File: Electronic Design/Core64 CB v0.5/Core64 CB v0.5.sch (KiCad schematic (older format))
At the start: 36 parts, among them J1 TSM-116-03-T-SV‎, J2 TSM-116-03-T-SV‎, U1 SI7210-B-01, U2 SI7210-B-02, U3 SI7210-B-03, U4 SI7210-B-04, U5 LTR-329ALS-01, U6 TS3A4751PWR, U7 TS3A4751PWR, X1 SFH11-NBPC-D03-ST-BK

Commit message: Core board redline refinement
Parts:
- added R1, R2, R3, R4: 10K, Resistor_SMD:R_0805_2012Metric, symbol Device:R_Small
- C5: value 1uF -> 0.1uF
- J1, J2: value TSM-116-03-T-SV‎ -> Digi-Key 77311-420-36LF-ND; footprint Connector_PinHeader_2.54mm:PinHeader_1x16_P2.54mm_Vertical_SMD_and_TH_Pin1Right -> Connector_PinHeader_2.54mm:PinHeader_1x18_P2.54mm_Vertical_SMD_and_TH_Pin1Right; symbol Connector:Conn_01x16_Male -> Connector:Conn_01x18_Male
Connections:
- wire segments 183 -> 201
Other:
- note added: "AMBIENT LIGHT SENSOR I2C 0x29"
- note added: "NOTE: These GPIO will be\nused by Core Plane Select\nif that option is enabled."
- note added: "REQUIRED: CONFIGURE FOR ONE CORE PLANE"
- note added: "SILKSCREEN:\n5V0\nGND\nXT3,7\nXT2,6\nXT1,5\nXT0,4\nXB0\nXB1\nXB2\nXB3\nXB4\nXB5\nXB6\nXB7\nP1/IO1\nP2/IO2\nP3\nP4"
- note added: "SILKSCREEN:\nLSIG\nUSER\nYL0\nYL1\nYL2\nYL3\nYL4,6\nYL5,7\nSEN1\nSEN2\nSCL\nSDA\n3V3\nGNDD\nP8\nP7\nP6\nP5"
- note added: "STEP 3: Install two quad switches\nand two decoupling caps."
- note added: "STEP 4: Modify sense wire\nrouting through connectors."
- note added: "STEP 5 (LOGIC BOARD):\nSee instructions on Logic Board."
- note removed: "AUTOMATIC LIGHT SENSOR I2C 0x29"
- note removed: "Ceramic"
- note removed: "DEFAULT FOR ONE CORE PLANE ONLY"
- note removed: "SILKSCREEN:\nXT3,7\nXT2,6\nXT1,5\nXT0,4\nXB0\nXB1\nXB2\nXB3\nXB4\nXB5\nXB6\nXB7\nP1/IO1\nP2/IO2\nP3\nP4"
- note removed: "SILKSCREEN:\nYL0\nYL1\nYL2\nYL3\nYL4,6\nYL5,7\nSEN1\nSEN2\nSCL\nSDA\n3V3\nGNDD\nP8\nP7\nP6\nP5"
- note removed: "STEP 3:\nInstall two quad switches and two decoupling caps."
- moved on the sheet: C1, C5, X1

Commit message: Update core grid to 6.75mm square
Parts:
- CM1: footprint Core_Memory_8x8_Array:core_64_x6.7_y6.5mm_v0.3_front_facing -> Core_Memory_8x8_Array:core_64_6.75mm_square_v0.5_front_facing
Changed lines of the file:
@@
 F 0 "CM1" H 3650 2500 50  0000 C CNN
 F 1 "Core_Memory_8x8_Array_Front_Facing" H 4300 900 50  0000 C CNN
-F 2 "Core_Memory_8x8_Array:core_64_x6.7_y6.5mm_v0.3_front_facing" H 4350 1900 50  0001 C CNN
+F 2 "Core_Memory_8x8_Array:core_64_6.75mm_square_v0.5_front_facing" H 4350 1900 50  0001 C CNN
 F 3 "" H 4350 1900 50  0001 C CNN
 	1    4300 1850

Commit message: Update CB to be compatible with LM V0.1
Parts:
- J1, J2: footprint Connector_PinHeader_2.54mm:PinHeader_1x18_P2.54mm_Vertical_SMD_and_TH_Pin1Right -> Connector_PinHeader_2.54mm:PinHeader_1x20_P2.54mm_Vertical_SMD_and_TH_Pin1Right; symbol Connector:Conn_01x18_Male -> Connector:Conn_01x20_Male
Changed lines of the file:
@@
 Text GLabel 3950 900  1    50   Input ~ 0
 XT0-4
+Text GLabel 6700 1750 0    50   Output ~ 0
+XB3
+Text GLabel 6700 1650 0    50   Output ~ 0
+XB2
+Text GLabel 6700 1550 0    50   Output ~ 0
+XB1
+Text GLabel 6700 1450 0    50   Output ~ 0
+XB0
 Text GLabel 6700 1850 0    50   Output ~ 0
-XB3
-Text GLabel 6700 1750 0    50   Output ~ 0
-XB2
-Text GLabel 6700 1650 0    50   Output ~ 0
-XB1
-Text GLabel 6700 1550 0    50   Output ~ 0
-XB0
+XB4
 Text GLabel 6700 1950 0    50   Output ~ 0
-XB4
+XB5
 Text GLabel 6700 2050 0    50   Output ~ 0
-XB5
+XB6
 Text GLabel 6700 2150 0    50   Output ~ 0
-XB6
-Text GLabel 6700 2250 0    50   Output ~ 0
 XB7
-Text GLabel 6700 1450 0    50   Output ~ 0
+Text GLabel 6700 1350 0    50   Output ~ 0
 H_XT0-4
-Text GLabel 6700 1350 0    50   Output ~ 0
+Text GLabel 6700 1250 0    50   Output ~ 0
 H_XT1-5
-Text GLabel 6700 1250 0    50   Output ~ 0
+Text GLabel 6700 1150 0    50   Output ~ 0
 H_XT2-6
-Text GLabel 6700 1150 0    50   Output ~ 0
+Text GLabel 6700 1050 0    50   Output ~ 0
 H_XT3-7
 Wire Wire Line
@@
 Connection ~ 4250 1000
 Wire Wire Line
+	6700 1050 6950 1050
+Wire Wire Line
 	6700 1150 6950 1150
 Wire Wire Line
@@
 Wire Wire Line
 	6700 1350 6950 1350
-Wire Wire Line
-	6700 1450 6950 1450
 Text GLabel 3600 2200 0    50   Input ~ 0
 YL7
@@
 Text GLabel 3600 1500 0    50   Input ~ 0
 YL0
+Text GLabel 2150 1200 2    50   Output ~ 0
+H_YL1
+Text GLabel 2150 1100 2    50   Output ~ 0
+H_YL0
 Text GLabel 2150 1300 2    50   Output ~ 0
-H_YL1
-Text GLabel 2150 1200 2    50   Output ~ 0
-H_YL0
+H_YL2
 Text GLabel 2150 1400 2    50   Output ~ 0
-H_YL2
+H_YL3
 Text GLabel 2150 1500 2    50   Output ~ 0
-H_YL3
+YL4
 Text GLabel 2150 1600 2    50   Output ~ 0
-YL4
+YL5
 Text GLabel 2150 1700 2    50   Output ~ 0
-YL5
+YL6
 Text GLabel 2150 1800 2    50   Output ~ 0
-YL6
-Text GLabel 2150 1900 2    50   Output ~ 0
 YL7
 Wire Wire Line
-	2100 1600 2100 1800
-Wire Wire Line
-	2100 1800 2150 1800
-Wire Wire Line
-	2150 1200 1500 1200
+	2100 1500 2100 1700
+Wire Wire Line
+	2100 1700 2150 1700
+Wire Wire Line
+	2150 1100 1500 1100
+Wire Wire Line
+	1500 1200 2150 1200
 Wire Wire Line
 	1500 1300 2150 1300
 Wire Wire Line
-	1500 1400 2150 1400
-Wire Wire Line
-	2150 1500 1500 1500
-Wire Wire Line
-	2150 1600 2100 1600
-Wire Wire Line
-	2100 1600 1500 1600
-Connection ~ 2100 1600
+	2150 1400 1500 1400
+Wire Wire Line
+	2150 1500 2100 1500
+Wire Wire Line
+	2100 1500 1500 1500
+Connection ~ 2100 1500
 Wire Wire Line
 	5350 1900 5000 1900
@@
 	5000 2200 5050 2200
 Wire Wire Line
-	2050 1900 2150 1900
-Wire Wire Line
-	2050 1700 2050 1900
-Wire Wire Line
-	2150 1700 2050 1700
+	2050 1800 2150 1800
+Wire Wire Line
+	2050 1600 2050 1800
+Wire Wire Line
+	2150 1600 2050 1600
 Text Notes 1150 2550 2    50   ~ 0
 SILKSCREEN:\nLSIG\nUSER\nYL0\nYL1\nYL2\nYL3\nYL4,6\nYL5,7\nSEN1\nSEN2\nSCL\nSDA\n3V3\nGNDD\nP8\nP7\nP6\nP5
 Wire Wire Line
-	2050 1700 1500 1700
-Connection ~ 2050 1700
-Wire Wire Line
-	6700 2250 6950 2250
+	2050 1600 1500 1600
+Connection ~ 2050 1600
 Wire Wire Line
 	6700 2150 6950 2150
-$Comp
-L Connector:Conn_01x18_Male J2
+Wire Wire Line
+	6700 2050 6950 2050
+$Comp
+L Connector:Conn_01x20_Male J2
 U 1 1 5E723F12
 P 7150 1750
 F 0 "J2" H 7150 2700 50  0000 C CNN
 F 1 "Digi-Key 77311-420-36LF-ND" H 8000 2700 50  0000 C CNN
-F 2 "Connector_PinHeader_2.54mm:PinHeader_1x18_P2.54mm_Vertical_SMD_and_TH_Pin1Right" H 7150 1750 50  0001 C CNN
+F 2 "Connector_PinHeader_2.54mm:PinHeader_1x20_P2.54mm_Vertical_SMD_and_TH_Pin1Right" H 7150 1750 50  0001 C CNN
 F 3 "~" H 7150 1750 50  0001 C CNN
 	1    7150 1750
@@
 	3850 2550 3850 2500
 Wire Wire Line
+	6950 1450 6700 1450
+Wire Wire Line
 	6950 1550 6700 1550
 Wire Wire Line
 	6950 1650 6700 1650
 Wire Wire Line
-	6950 1750 6700 1750
-Wire Wire Line
-	6700 1850 6950 1850
-Wire Wire Line
-	6950 1950 6700 1950
-Wire Wire Line
-	6700 2050 6950 2050
-Text GLabel 1650 1900 2    50   Input ~ 0
+	6700 1750 6950 1750
+Wire Wire Line
+	6950 1850 6700 1850
+Wire Wire Line
+	6700 1950 6950 1950
+Text GLabel 1650 1800 2    50   Input ~ 0
 SENSE1
-Text GLabel 1650 1800 2    50   Input ~ 0
+Text GLabel 1650 1700 2    50   Input ~ 0
 SENSE2
 Wire Wire Line
@@
 	3550 2450 3500 2450
 Wire Wire Line
-	1650 1900 1500 1900
-Wire Wire Line
-	2450 2300 2450 2400
-Wire Wire Line
-	1500 2200 1650 2200
-Wire Wire Line
-	1500 2300 2450 2300
-Wire Wire Line
-	1500 2400 1900 2400
-Wire Wire Line
-	1900 2500 1500 2500
-Wire Wire Line
-	1500 2600 1900 2600
-Wire Wire Line
-	1900 2700 1500 2700
-Wire Wire Line
-	1500 1800 1650 1800
+	1650 1800 1500 1800
+Wire Wire Line
+	2450 2200 2450 2300
+Wire Wire Line
+	1500 2100 1650 2100
+Wire Wire Line
+	1500 2200 2450 2200
+Wire Wire Line
+	1500 2300 1900 2300
+Wire Wire Line
+	1900 2400 1500 2400
+Wire Wire Line
+	1500 2500 1900 2500
+Wire Wire Line
+	1900 2600 1500 2600
+Wire Wire Line
+	1500 1700 1650 1700
+Text GLabel 1650 1900 2    50   BiDi ~ 0
+I2C_CLOCK
 Text GLabel 1650 2000 2    50   BiDi ~ 0
-I2C_CLOCK
-Text GLabel 1650 2100 2    50   BiDi ~ 0
 I2C_DATA
 Wire Wire Line
+	1500 1900 1650 1900
+Wire Wire Line
 	1500 2000 1650 2000
-Wire Wire Line
-	1500 2100 1650 2100
-Text GLabel 1650 2200 2    50   Input ~ 0
+Text GLabel 1650 2100 2    50   Input ~ 0
 3V3_800mA
 Text Notes 1650 4500 0    50   ~ 0
@@
 Text Notes 3300 4700 0    50   ~ 0
 I2C configurable hall sensors, not just a switch.\nSilicon Labs SI7210-B-01-IVR through 04-IVR\nLow (push-pull) up to 20 mT, SOT23-5\nhttps://www.digikey.com/product-detail/en/silicon-labs/SI7210-B-04-IVR/336-4129-1-ND/7648844
-Text Notes 2350 2850 0    50   ~ 0
+Text Notes 2350 2750 0    50   ~ 0
 DIGITAL\nLOGIC\nGROUND
 $Comp
@@
 Wire Wire Line
 	9050 1400 9200 1400
-Text GLabel 6950 2800 2    50   Input ~ 0
+Text GLabel 6950 2850 2    50   Input ~ 0
 SAO_GPIO2
 Text GLabel 6950 2950 2    50   Input ~ 0
 SAO_GPIO1
 Wire Wire Line
-	6850 2800 6950 2800
-Wire Wire Line
-	6850 2450 6850 2800
+	6850 2850 6950 2850
+Wire Wire Line
+	6850 2350 6850 2850
 Wire Wire Line
 	6950 2950 6650 2950
@@
 L power:GNDD #PWR05
 U 1 1 5E880DFA
-P 2450 2400
-F 0 "#PWR05" H 2450 2150 50  0001 C CNN
-F 1 "GNDD" H 2454 2245 50  0000 C CNN
-F 2 "" H 2450 2400 50  0001 C CNN
-F 3 "" H 2450 2400 50  0001 C CNN
-	1    2450 2400
-	1    0    0    -1
-$EndComp
+P 2450 2300
+F 0 "#PWR05" H 2450 2050 50  0001 C CNN
+F 1 "GNDD" H 2454 2145 50  0000 C CNN
+F 2 "" H 2450 2300 50  0001 C CNN
+F 3 "" H 2450 2300 50  0001 C CNN
+	1    2450 2300
+	1    0    0    -1
+$EndComp
+Wire Wire Line
+	6350 2450 6950 2450
+Wire Wire Line
+	6350 2350 6850 2350
+Connection ~ 6850 2350
+Wire Wire Line
+	6850 2350 6950 2350
 Wire Wire Line
 	6350 2550 6950 2550
-Wire Wire Line
-	6350 2450 6850 2450
-Connection ~ 6850 2450
-Wire Wire Line
-	6850 2450 6950 2450
-Wire Wire Line
-	6350 2650 6950 2650
 Text Notes 9050 1300 0    50   ~ 0
 SILKSCREEN FRONT AND BACK: \nSAO, GNDD, 3V3, SDA,SCL\nGPIO1, GPIO2
@@
 	1    0    0    -1
 $EndComp
+Text GLabel 1900 2300 2    50   Output ~ 0
+PLANE_8
 Text GLabel 1900 2400 2    50   Output ~ 0
-PLANE_8
+PLANE_7
 Text GLabel 1900 2500 2    50   Output ~ 0
-PLANE_7
+PLANE_6
 Text GLabel 1900 2600 2    50   Output ~ 0
-PLANE_6
-Text GLabel 1900 2700 2    50   Output ~ 0
 PLANE_5
-Text GLabel 6350 2650 0    50   Output ~ 0
+Text GLabel 6350 2550 0    50   Output ~ 0
 PLANE_4
-Text GLabel 6350 2550 0    50   Output ~ 0
+Text GLabel 6350 2450 0    50   Output ~ 0
 PLANE_3
-Text GLabel 6350 2450 0    50   Output ~ 0
+Text GLabel 6350 2350 0    50   Output ~ 0
 PLANE_2
-Text GLabel 6350 2350 0    50   Output ~ 0
+Text GLabel 6350 2250 0    50   Output ~ 0
 PLANE_1
 Wire Wire Line
-	6950 2350 6650 2350
-Wire Wire Line
-	6650 2950 6650 2350
-Connection ~ 6650 2350
-Wire Wire Line
-	6650 2350 6350 2350
+	6950 2250 6650 2250
+Wire Wire Line
+	6650 2950 6650 2250
+Connection ~ 6650 2250
+Wire Wire Line
+	6650 2250 6350 2250
 $Comp
 L Device:C C6
@@
 Wire Wire Line
 	7700 4300 8600 4300
-NoConn ~ 1500 1100
-$Comp
-L Connector:Conn_01x18_Male J1
+NoConn ~ 1500 1000
+$Comp
+L Connector:Conn_01x20_Male J1
 U 1 1 5E72894A
 P 1300 1800
 F 0 "J1" H 1300 2750 50  0000 C CNN
 F 1 "Digi-Key 77311-420-36LF-ND" H 2150 2750 50  0000 C CNN
-F 2 "Connector_PinHeader_2.54mm:PinHeader_1x18_P2.54mm_Vertical_SMD_and_TH_Pin1Right" H 1300 1800 50  0001 C CNN
+F 2 "Connector_PinHeader_2.54mm:PinHeader_1x20_P2.54mm_Vertical_SMD_and_TH_Pin1Right" H 1300 1800 50  0001 C CNN
 F 3 "~" H 1300 1800 50  0001 C CNN
 	1    1300 1800
 	1    0    0    -1
 $EndComp
-NoConn ~ 6950 1050
 NoConn ~ 6950 950
-NoConn ~ 1500 1000
+NoConn ~ 6950 850
+NoConn ~ 1500 900
 $EndSCHEMATC

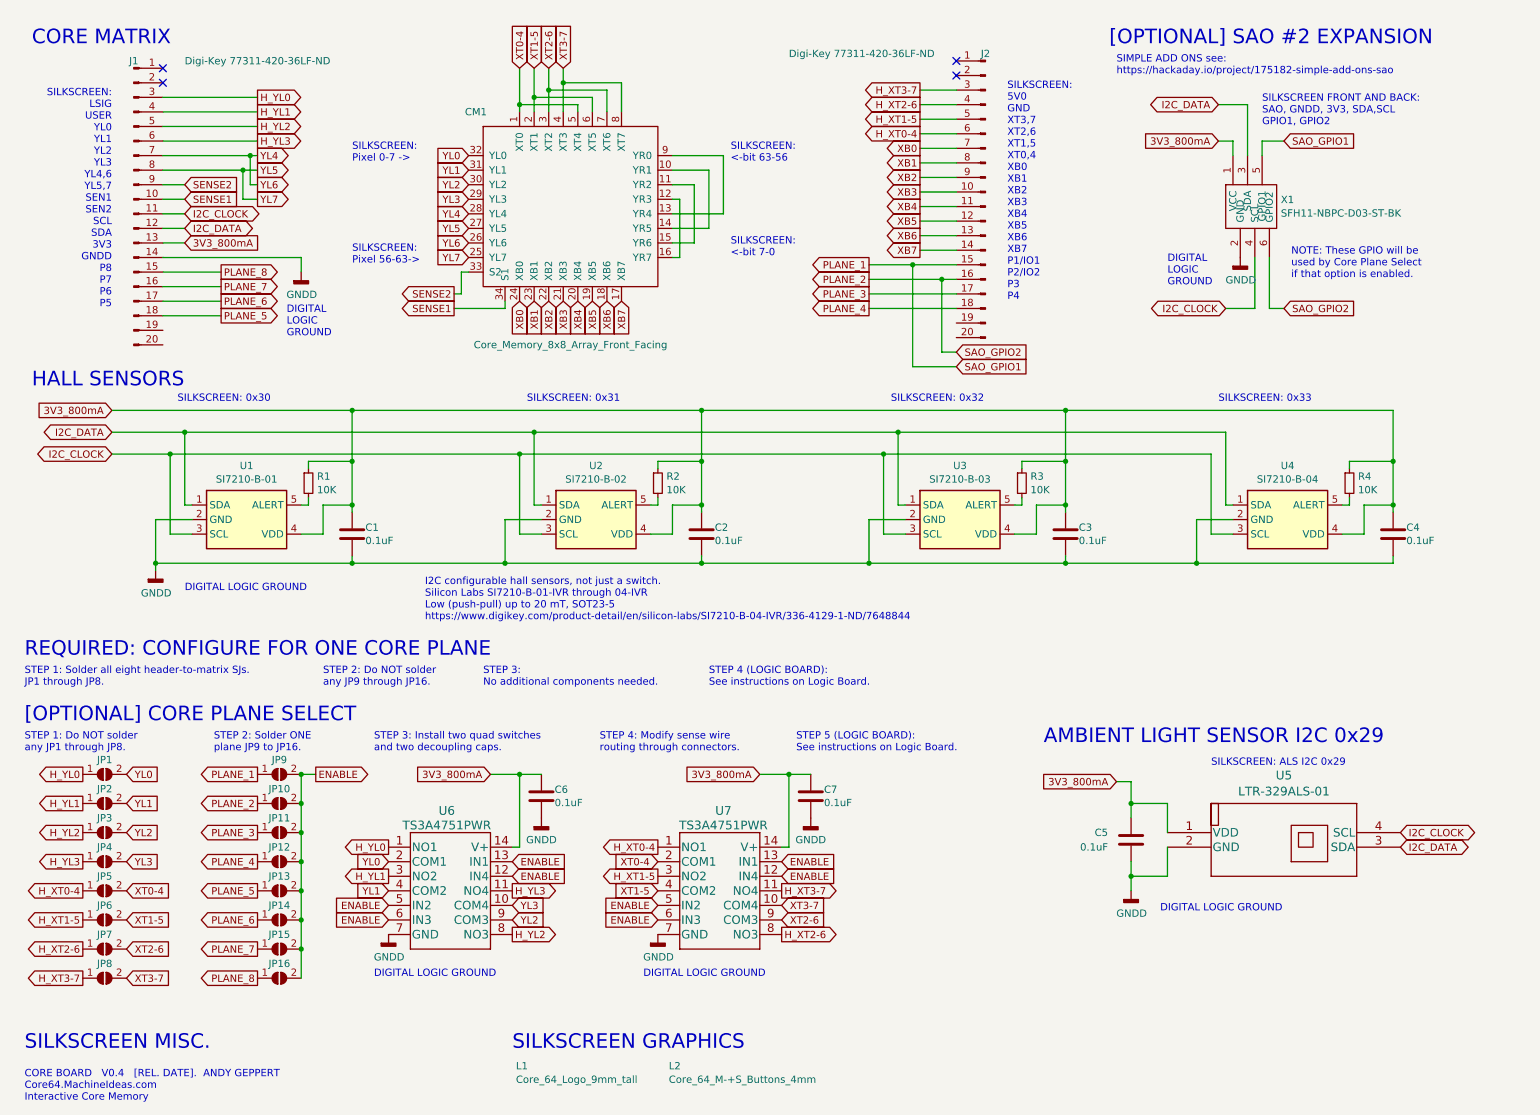
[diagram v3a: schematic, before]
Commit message: Complete draft V0.5 Core Board changes, new ALS, hall switches
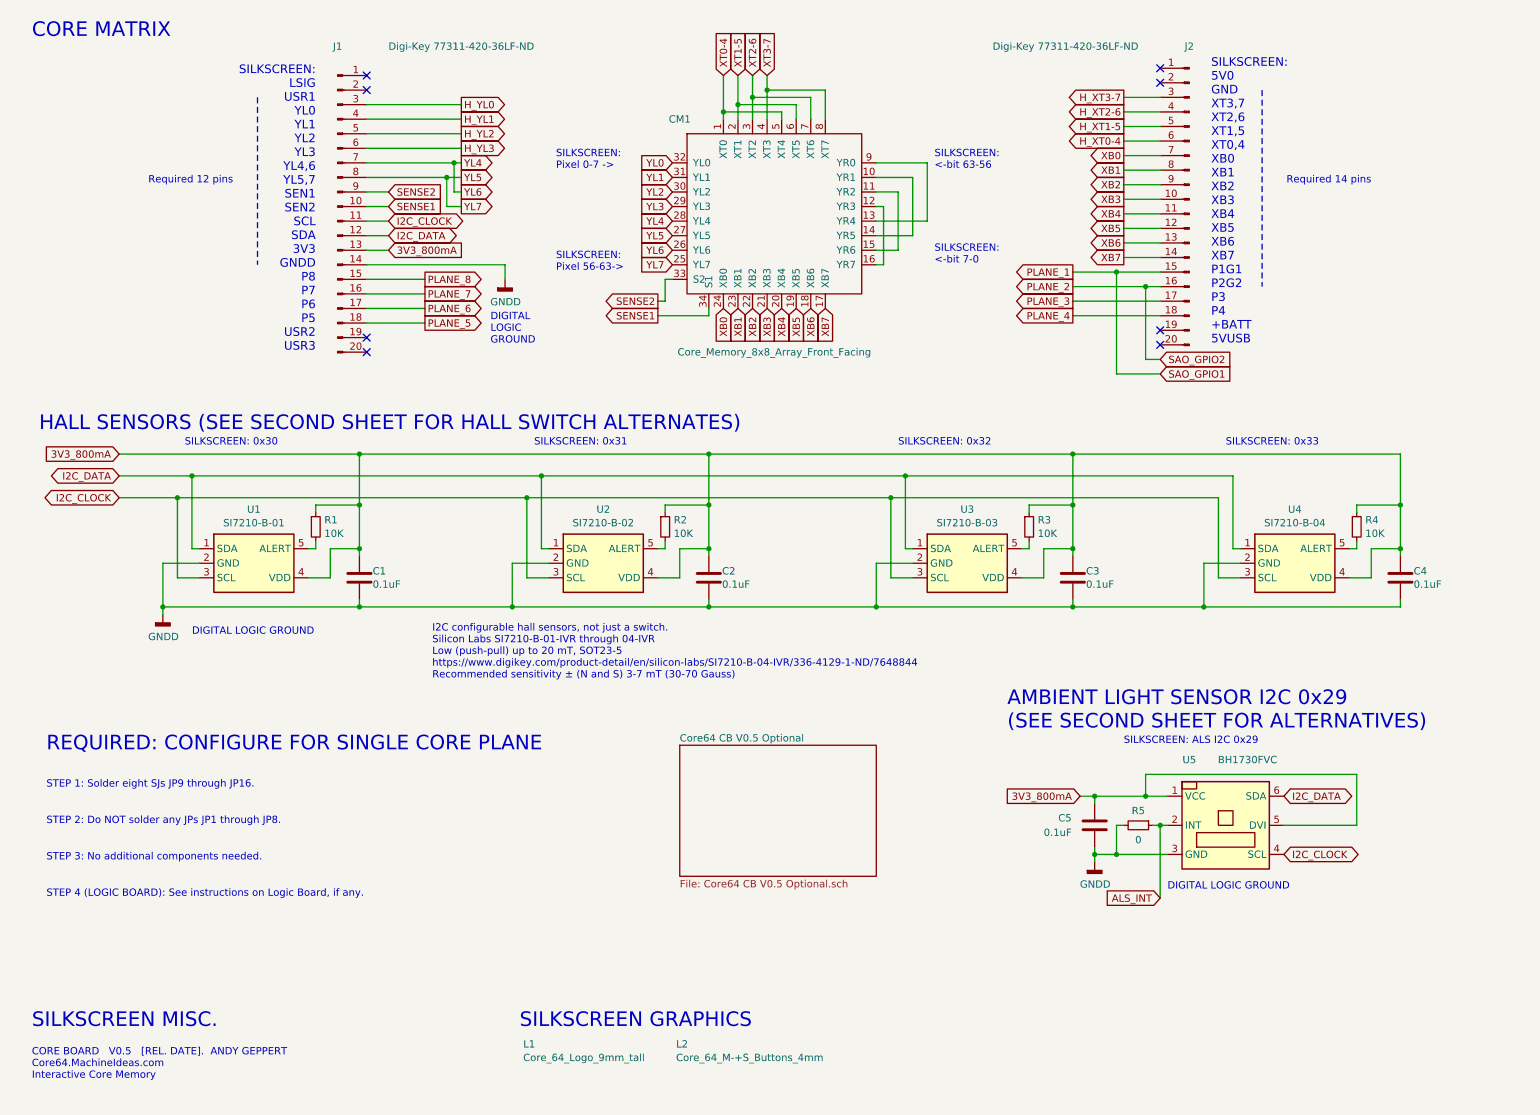
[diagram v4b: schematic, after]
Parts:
- removed C6, C7: 0.1uF, Capacitor_SMD:C_0805_2012Metric, symbol Device:C
- removed JP1, JP2, JP3, JP4, JP5, JP6, JP7, JP8: SolderJumper_2_Bridged, Jumper:SolderJumper-2_P1.3mm_Open_Pad1.0x1.5mm, symbol Jumper:SolderJumper_2_Open
- removed JP10, JP11, JP12, JP13, JP14, JP15, JP16, JP9: SolderJumper_2_Open, Jumper:SolderJumper-2_P1.3mm_Open_Pad1.0x1.5mm, symbol Jumper:SolderJumper_2_Open
- removed U5: LTR-329ALS-01, LiteOn_LTR-329ALS:LTR-329ALS-01, symbol LiteOn_LTR-329ALS:LTR-329ALS-01
- removed U6, U7: TS3A4751PWR, TI_TS3A4751PWR:TS3A4751PWR, symbol TI_TS3A4751PWR:TS3A4751PWR
- removed X1: SFH11-NBPC-D03-ST-BK, badgelife_sao_v169bis:Badgelife-SAOv169-BADGE-2x3, symbol Core64-CB-v0.5-rescue:Badgelife_sao_connector_v169bis-badgelife_shitty_addon_v1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
- added R5: 0, Resistor_SMD:R_0805_2012Metric, symbol Device:R_Small
- added U5: BH1730FVC, ALS_BH1730:BH1730-backside, symbol Core_64_KiCad_Library:BH1730FVC
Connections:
- net 3V3_800mA: now also U5.1 (VCC), U5.5 (DVI)
- net GNDD: now also R5.2, U5.3 (GND)
- net I2C_CLOCK: now also U5.4 (SCL)
- net I2C_DATA: now also U5.6 (SDA)
- new net ALS_INT: R5.1, U5.2 (INT)
- no-connect marks 4 -> 8
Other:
- note added: "AMBIENT LIGHT SENSOR I2C 0x29\n(SEE SECOND SHEET FOR ALTERNATIVES)"
- note added: "CORE BOARD V0.5 [REL. DATE]. ANDY GEPPERT \nCore64.MachineIdeas.com\nInteractive Core Memory"
- note added: "HALL SENSORS (SEE SECOND SHEET FOR HALL SWITCH ALTERNATES)"
- note added: "I2C configurable hall sensors, not just a switch.\nSilicon Labs SI7210-B-01-IVR through 04-IVR\nLow (push-pull) up to 20 mT, SOT23-5\nhttps://www.digikey.com/product-detail/en/silicon-labs/SI7210-B-04-IVR/336-4129-1-ND/7648844\nRecommended sensitivity ± (N and S) 3-7 mT (30-70 Gauss)"
- note added: "REQUIRED: CONFIGURE FOR SINGLE CORE PLANE"
- note added: "Required 12 pins"
- note added: "Required 14 pins"
- note added: "SILKSCREEN:\n5V0\nGND\nXT3,7\nXT2,6\nXT1,5\nXT0,4\nXB0\nXB1\nXB2\nXB3\nXB4\nXB5\nXB6\nXB7\nP1G1\nP2G2\nP3\nP4\n+BATT\n5VUSB"
- note added: "SILKSCREEN:\nLSIG\nUSR1\nYL0\nYL1\nYL2\nYL3\nYL4,6\nYL5,7\nSEN1\nSEN2\nSCL\nSDA\n3V3\nGNDD\nP8\nP7\nP6\nP5\nUSR2\nUSR3"
- note added: "STEP 1: Solder eight SJs JP9 through JP16."
- note added: "STEP 2: Do NOT solder any JPs JP1 through JP8."
- note added: "STEP 3: No additional components needed."
- note added: "STEP 4 (LOGIC BOARD): See instructions on Logic Board, if any."
- note removed: "AMBIENT LIGHT SENSOR I2C 0x29"
- note removed: "CORE BOARD V0.4 [REL. DATE]. ANDY GEPPERT \nCore64.MachineIdeas.com\nInteractive Core Memory"
- note removed: "HALL SENSORS"
- note removed: "I2C configurable hall sensors, not just a switch.\nSilicon Labs SI7210-B-01-IVR through 04-IVR\nLow (push-pull) up to 20 mT, SOT23-5\nhttps://www.digikey.com/product-detail/en/silicon-labs/SI7210-B-04-IVR/336-4129-1-ND/7648844"
- note removed: "NOTE: These GPIO will be\nused by Core Plane Select\nif that option is enabled."
- note removed: "REQUIRED: CONFIGURE FOR ONE CORE PLANE"
- note removed: "SILKSCREEN FRONT AND BACK: \nSAO, GNDD, 3V3, SDA,SCL\nGPIO1, GPIO2"
- note removed: "SILKSCREEN:\n5V0\nGND\nXT3,7\nXT2,6\nXT1,5\nXT0,4\nXB0\nXB1\nXB2\nXB3\nXB4\nXB5\nXB6\nXB7\nP1/IO1\nP2/IO2\nP3\nP4"
- note removed: "SILKSCREEN:\nLSIG\nUSER\nYL0\nYL1\nYL2\nYL3\nYL4,6\nYL5,7\nSEN1\nSEN2\nSCL\nSDA\n3V3\nGNDD\nP8\nP7\nP6\nP5"
- note removed: "SIMPLE ADD ONS see:\nhttps://hackaday.io/project/175182-simple-add-ons-sao"
- note removed: "STEP 1: Do NOT solder\nany JP1 through JP8."
- note removed: "STEP 1: Solder all eight header-to-matrix SJs.\nJP1 through JP8."
- note removed: "STEP 2: Do NOT solder\nany JP9 through JP16."
- note removed: "STEP 2: Solder ONE \nplane JP9 to JP16."
- note removed: "STEP 3: Install two quad switches\nand two decoupling caps."
- note removed: "STEP 3:\nNo additional components needed."
- note removed: "STEP 4 (LOGIC BOARD):\nSee instructions on Logic Board."
- note removed: "STEP 4: Modify sense wire\nrouting through connectors."
- note removed: "STEP 5 (LOGIC BOARD):\nSee instructions on Logic Board."
- note removed: "[OPTIONAL] CORE PLANE SELECT"
- note removed: "[OPTIONAL] SAO #2 EXPANSION"
- moved on the sheet: C1, C2, C3, C4, CM1, J1, J2, R1, R2, R3, R4, U1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
